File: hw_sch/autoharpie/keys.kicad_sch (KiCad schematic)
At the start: 12 parts, among them J7 Conn_01x10_Socket, J8 Conn_01x04_Pin, J9 Conn_01x10_Pin, U8 MSP430FR2633IDAR, Y1 32.768KHz

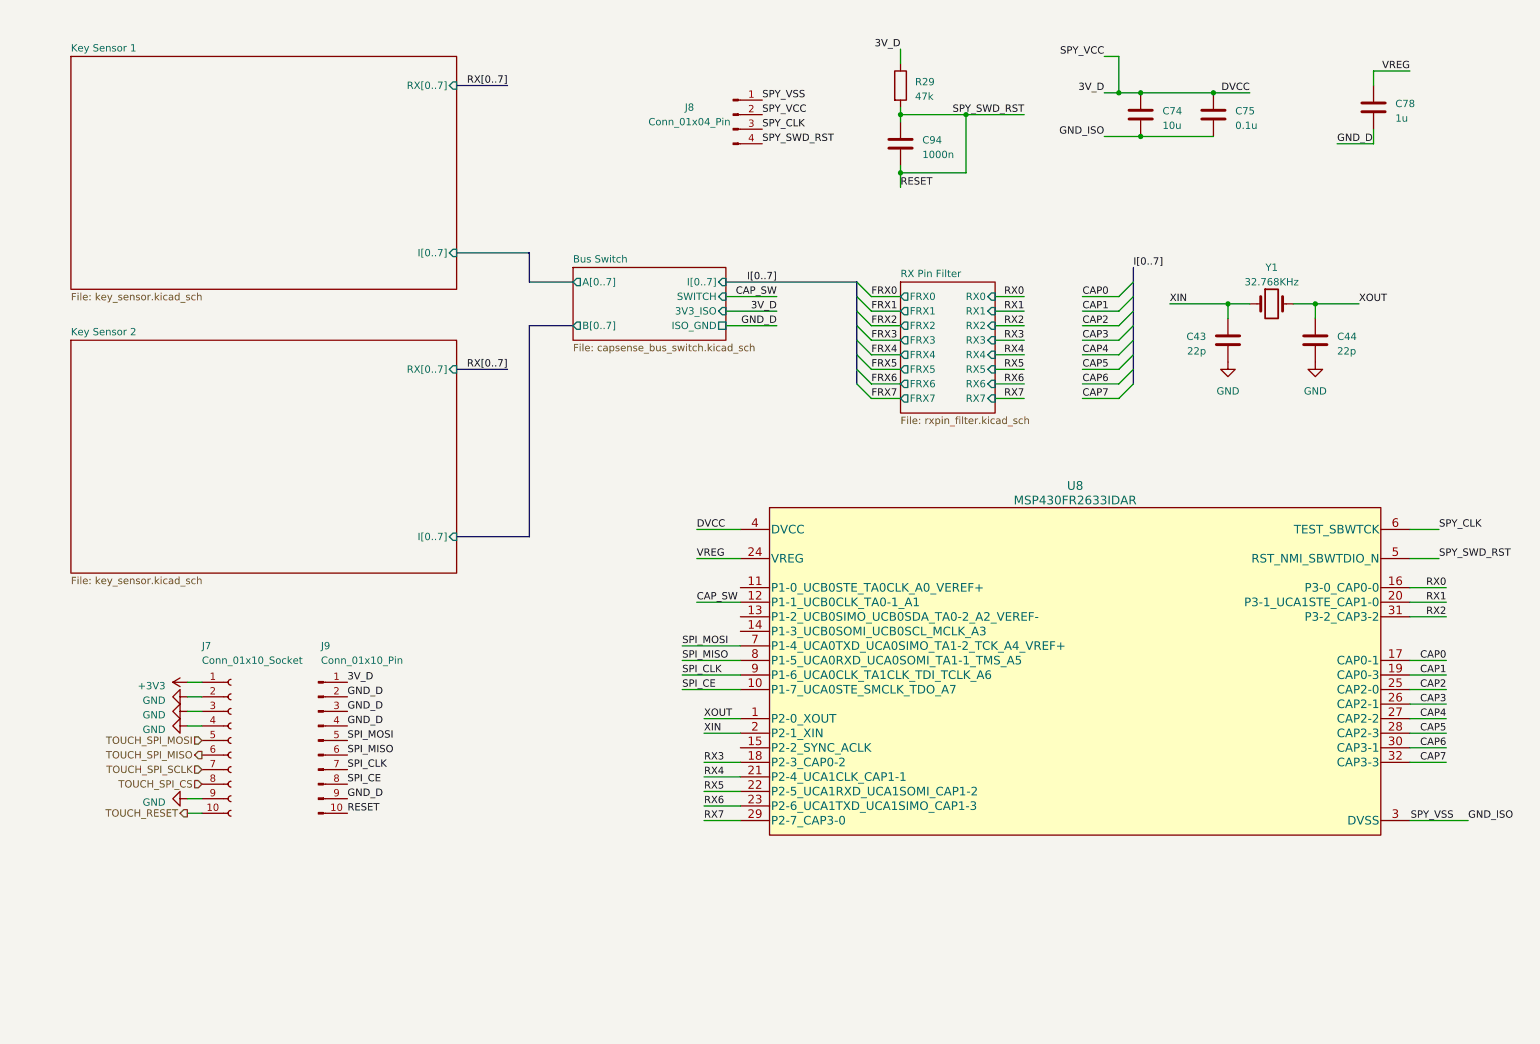
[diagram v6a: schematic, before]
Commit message: seperate keypad
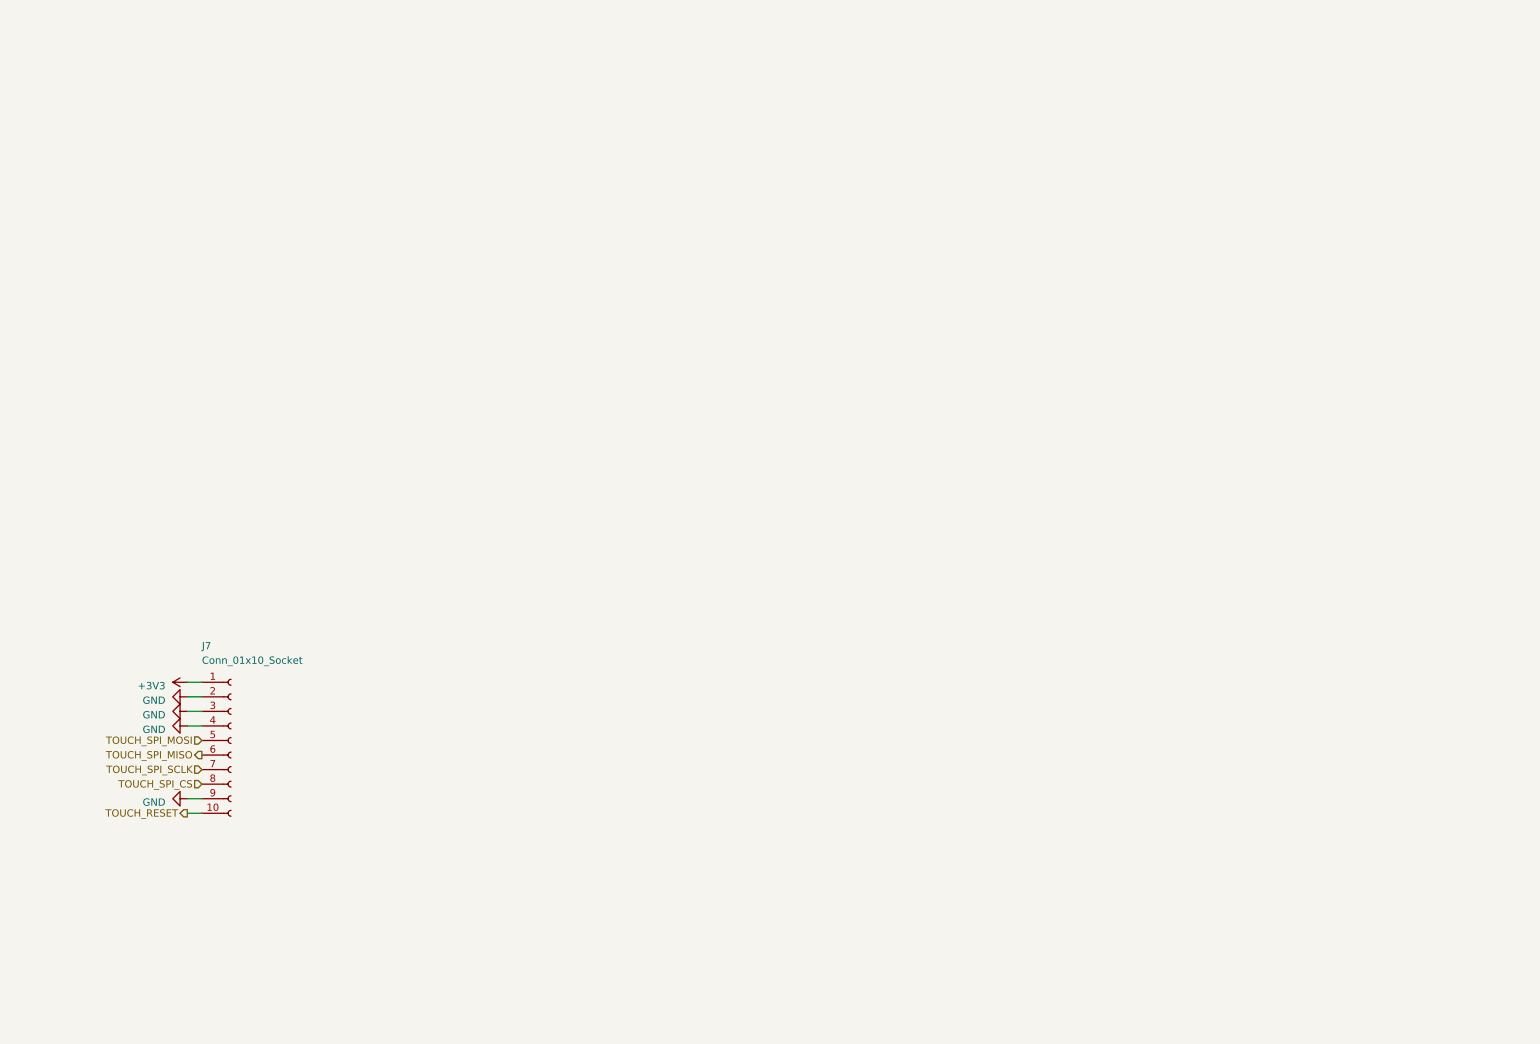
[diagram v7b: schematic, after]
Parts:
- removed C43, C44: 22p, symbol Device:C
- removed C74: 10u, symbol Device:C
- removed C75: 0.1u, symbol Device:C
- removed C78: 1u, symbol Device:C
- removed C94: 1000n, symbol Device:C
- removed J8: Conn_01x04_Pin, symbol Connector:Conn_01x04_Pin
- removed J9: Conn_01x10_Pin, symbol Connector:Conn_01x10_Pin
- removed R29: 47k, symbol Device:R
- removed U8: MSP430FR2633IDAR, DA0032A_N, symbol 2023-03-09_01-52-04:MSP430FR2633IDAR
- removed Y1: 32.768KHz, symbol Device:Crystal
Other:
- removed sheet Bus Switch
- removed sheet Key Sensor 1
- removed sheet Key Sensor 2
- removed sheet RX Pin Filter

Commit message: finish keypad
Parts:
- removed J7: Conn_01x10_Socket, Connector_FFC-FPC:Hirose_FH12-35S-0.5SH_1x35-1MP_P0.50mm_Horizontal, symbol Connector:Conn_01x10_Socket
- added C1: 1u, Capacitor_SMD:C_0402_1005Metric, symbol Device:C
- added C2: 10u, Capacitor_SMD:C_1206_3216Metric, symbol Device:C
- added C3: 0.1u, Capacitor_SMD:C_0402_1005Metric, symbol Device:C
- added C4: 1000n, Capacitor_SMD:C_0201_0603Metric, symbol Device:C
- added C5, C6: 22p, Capacitor_SMD:C_0402_1005Metric, symbol Device:C
- added D1: LED, LED_SMD:LED_0402_1005Metric, symbol Device:LED
- added J1: Conn_01x04_Pin, Connector_PinHeader_2.54mm:PinHeader_1x04_P2.54mm_Vertical, symbol Connector:Conn_01x04_Pin
- added R1: 470, Resistor_SMD:R_0603_1608Metric, symbol Device:R
- added R2: 47k, Resistor_SMD:R_0603_1608Metric, symbol Device:R
- added SW1: SW_Push, Button_Switch_SMD:SW_Push_SPST_NO_Alps_SKRK, symbol Switch:SW_Push
- added U1: MSP430FR2633IDAR, footprints:MSP430FR2633IDAR, symbol 2023-03-09_01-52-04:MSP430FR2633IDAR
- added Y1: 32.768KHz, Crystal:Crystal_SMD_MicroCrystal_CM9V-T1A-2Pin_1.6x1.0mm, symbol Device:Crystal
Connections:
- net +3V3: now also C2.1, C3.1, J1.2 (Pin_2), R2.1, U1.4 (DVCC)
- net GND: now also C1.2, C2.2, C3.2, C5.2, C6.2, D1.1 (K), J1.1 (Pin_1), U1.3 (DVSS)
- net TOUCH_SPI_CS: now also U1.10 (P1-7_UCA0STE_SMCLK_TDO_A7)
- net TOUCH_SPI_MISO: now also U1.8 (P1-5_UCA0RXD_UCA0SOMI_TA1-1_TMS_A5)
- net TOUCH_SPI_MOSI: now also U1.7 (P1-4_UCA0TXD_UCA0SIMO_TA1-2_TCK_A4_VREF+)
- net TOUCH_SPI_SCLK: now also U1.9 (P1-6_UCA0CLK_TA1CLK_TDI_TCLK_A6)
- new net: D1.2 (A), R1.2
- new net CAP0: U1.17 (CAP0-1)
- new net CAP1: U1.19 (CAP0-3)
- new net CAP2: U1.25 (CAP2-0)
- new net CAP3: U1.26 (CAP2-1)
- new net CAP4: U1.27 (CAP2-2)
- new net CAP5: U1.28 (CAP2-3)
- new net CAP6: U1.30 (CAP3-1)
- new net CAP7: U1.32 (CAP3-3)
- new net CAP_SW: U1.12 (P1-1_UCB0CLK_TA0-1_A1)
- new net RESET: C4.2, SW1.2
- new net RX0: U1.16 (P3-0_CAP0-0)
- new net RX1: U1.20 (P3-1_UCA1STE_CAP1-0)
- new net RX2: U1.31 (P3-2_CAP3-2)
- new net RX3: U1.18 (P2-3_CAP0-2)
- new net RX4: U1.21 (P2-4_UCA1CLK_CAP1-1)
- new net RX5: U1.22 (P2-5_UCA1RXD_UCA1SOMI_CAP1-2)
- new net RX6: U1.23 (P2-6_UCA1TXD_UCA1SIMO_CAP1-3)
- new net RX7: U1.29 (P2-7_CAP3-0)
- new net SPY_CLK: J1.3 (Pin_3), U1.6 (TEST_SBWTCK)
- new net SPY_SWD_RST: C4.1, J1.4 (Pin_4), R2.2, SW1.1, U1.5 (RST_NMI_SBWTDIO_N)
- new net STATUS_LED: R1.1, U1.11 (P1-0_UCB0STE_TA0CLK_A0_VEREF+)
- new net VREG: C1.1, U1.24 (VREG)
- new net XIN: C5.1, U1.2 (P2-1_XIN), Y1.1
- new net XOUT: C6.1, U1.1 (P2-0_XOUT), Y1.2
- no-connect marks 0 -> 3
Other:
- added sheet RX Pin Filter (rxpin_filter.kicad_sch)
